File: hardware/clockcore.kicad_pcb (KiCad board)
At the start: 2 copper layers, 75 x 40 mm, 38 parts, among them J1 Header, J2 USB_C_Receptacle_USB2.0, J3 JTAG Debug Header, Q1 MBT3904DW1T1G, SW1 Reset, SW2 Boot, U1 ESP32-WROOM-32, U2 DS1338Z-33+, U3 FT231XS, U4 USBLC6-4SC6, U5 ‎SN74HCT245PWR‎, Y1 32.768Hz, 12.5pF, 45kΩ

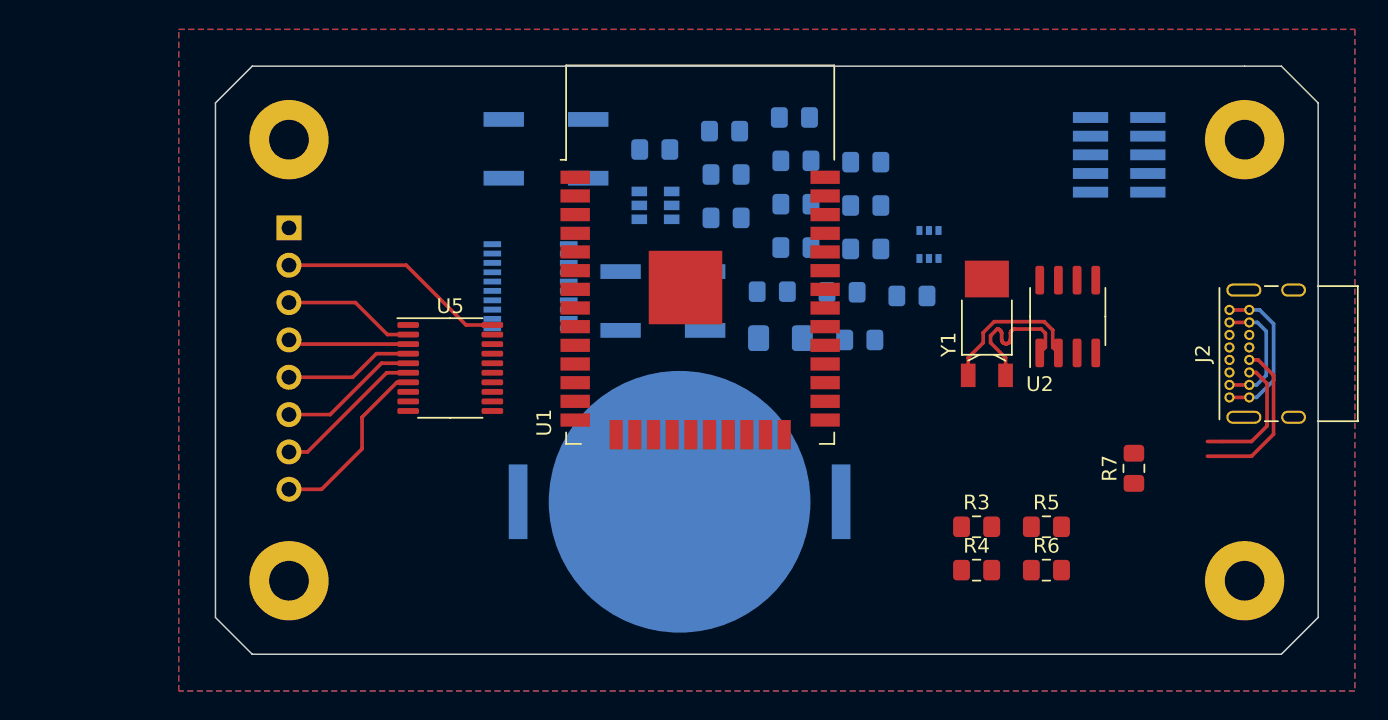
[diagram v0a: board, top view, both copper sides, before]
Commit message: finished schematic for clockcore, pcb layout todo
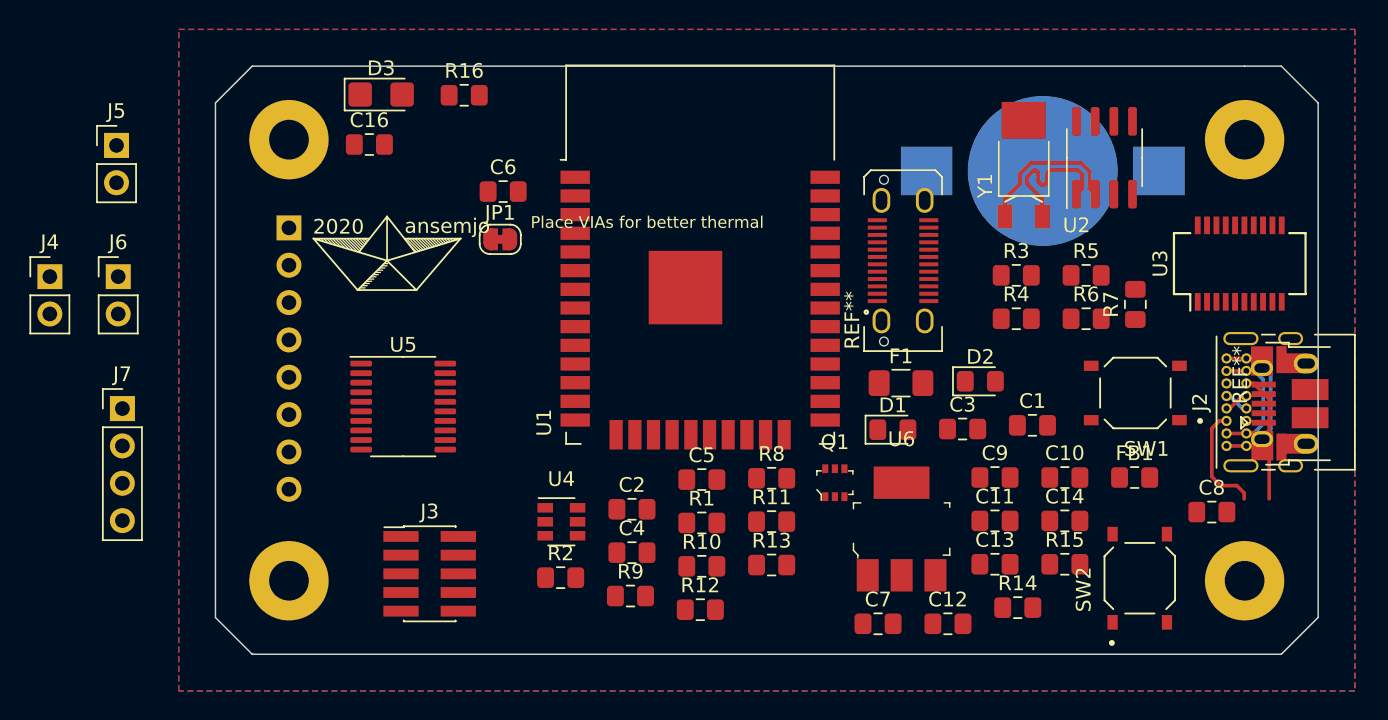
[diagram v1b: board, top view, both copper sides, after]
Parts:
- added A1: 2020, extra_libraries:AHOI, F.Cu at (96.7, 60.7)
- added C10: 4.7µF, Capacitor_SMD:C_0805_2012Metric_Pad1.15x1.40mm_HandSolder, F.Cu at (142.8, 75.5)
- added C11: 100nF, Capacitor_SMD:C_0805_2012Metric_Pad1.15x1.40mm_HandSolder, F.Cu at (138.0, 78.4)
- added C12: 10µF, Capacitor_SMD:C_0805_2012Metric_Pad1.15x1.40mm_HandSolder, F.Cu at (134.8, 85.4)
- added C13: 100nF, Capacitor_SMD:C_0805_2012Metric_Pad1.15x1.40mm_HandSolder, F.Cu at (138.0, 81.4)
- added C14: DNP/100nF, Capacitor_SMD:C_0805_2012Metric_Pad1.15x1.40mm_HandSolder, F.Cu at (142.8, 78.4)
- added C16: 1nF, Capacitor_SMD:C_0805_2012Metric_Pad1.15x1.40mm_HandSolder, F.Cu at (95.5, 52.8)
- added C6: 10nF, Capacitor_SMD:C_0805_2012Metric_Pad1.15x1.40mm_HandSolder, F.Cu at (104.6, 56.0)
- added C7: 4.7µF, Capacitor_SMD:C_0805_2012Metric_Pad1.15x1.40mm_HandSolder, F.Cu at (130.1, 85.4)
- added C8: 100nF, Capacitor_SMD:C_0805_2012Metric_Pad1.15x1.40mm_HandSolder, F.Cu at (152.8, 77.8)
- added C9: 4.7µF, Capacitor_SMD:C_0805_2012Metric_Pad1.15x1.40mm_HandSolder, F.Cu at (138.0, 75.5)
- added D3: Ambient Light Sensor, Diode_SMD:D_1206_3216Metric_Castellated, F.Cu at (96.3, 49.4)
- added FB1: BLM21PG221SZ1D, Inductor_SMD:L_0805_2012Metric_Pad1.15x1.40mm_HandSolder, F.Cu at (147.5, 75.5)
- added J4: 3.3V, Connector_PinHeader_2.54mm:PinHeader_1x02_P2.54mm_Vertical, F.Cu at (73.7, 61.8)
- added J5: 5V, Connector_PinHeader_2.54mm:PinHeader_1x02_P2.54mm_Vertical, F.Cu at (78.3, 52.9)
- added J6: I2C, Connector_PinHeader_2.54mm:PinHeader_1x02_P2.54mm_Vertical, F.Cu at (78.4, 61.8)
- added J7: Serial Prog, Connector_PinHeader_2.54mm:PinHeader_1x04_P2.54mm_Vertical, F.Cu at (78.7, 70.8)
- added JP1: Bridge, Jumper:SolderJumper-2_P1.3mm_Bridged_RoundedPad1.0x1.5mm, F.Cu at (104.4, 59.3)
- added R14: 10kΩ, Resistor_SMD:R_0805_2012Metric_Pad1.15x1.40mm_HandSolder, F.Cu at (139.6, 84.3)
- added R15: 10kΩ, Resistor_SMD:R_0805_2012Metric_Pad1.15x1.40mm_HandSolder, F.Cu at (142.8, 81.4)
- added R16: 4.7kΩ, Resistor_SMD:R_0805_2012Metric_Pad1.15x1.40mm_HandSolder, F.Cu at (101.9, 49.5)
- added REF**: USB_Micro-B_Amphenol_10103594-0001LF_Horizontal, Connector_USB:USB_Micro-B_Amphenol_10103594-0001LF_Horizontal, F.Cu at (158.1, 70.4)
- added REF**: USB_C_Receptacle_JAE_DX07S024WJ3R400, Connector_USB:USB_C_Receptacle_JAE_DX07S024WJ3R400, F.Cu at (131.8, 60.7)
- added U6: AP2114H-3_3TRG1, digikey-footprints:SOT-223, F.Cu at (131.7, 79.0)
- BT1: value 20mm Coin Cell -> 12mm Coin Cell; footprint Battery:BatteryHolder_Keystone_3034_1x20mm -> Battery:BatteryHolder_Keystone_3000_1x12mm
- C1, C2, C3, C4, C5, D1, D2, F1, Q1, R1, R10, R11, R12, R13, R2, R8, R9, U3, U4: moved to F.Cu
- J3: value JTAG Debug Header -> JTAG; moved to F.Cu
- SW1, SW2: footprint Button_Switch_SMD:SW_SPST_B3SL-1002P -> extra_libraries:SW_PTS526_SM08_SMTR2_LFS; moved to F.Cu
- moved J3 54.9 mm to (99.6, 82.0)
- moved SW2 49.8 mm to (147.9, 82.3), turned to 90 degrees
- moved U3 48.3 mm to (154.7, 60.9), turned to 90 degrees
- moved R12 34.1 mm to (118.0, 84.5)
- moved BT1 33.4 mm to (141.3, 54.6), turned to 0 degrees
- moved SW1 32.7 mm to (147.6, 69.7), turned to 180 degrees
- moved R9 32.3 mm to (113.2, 83.5)
- moved R2 29.8 mm to (108.5, 82.3)
- moved R10 28.3 mm to (118.1, 81.5)
- moved R13 28.1 mm to (122.8, 81.4)
- moved C4 26.5 mm to (113.3, 80.6)
- moved R1 22.6 mm to (118.1, 78.6)
- moved U4 22.5 mm to (108.5, 78.5)
- moved R11 22.4 mm to (122.8, 78.5)
- moved C2 20.8 mm to (113.3, 77.6)
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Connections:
- net FIL_SHDN renamed /FIL_SHDN
- net HV_BLANK renamed /HV_BLANK
- net HV_CLOCK renamed /HV_CLOCK
- net HV_DATA renamed /HV_DATA
- net HV_STROBE renamed /HV_STROBE
- net ~HV_SHDN~ renamed /~HV_SHDN~
- D1 pad 2: +3V3 -> Net-(D1-Pad2)
- J2 pad A4: Net-(F1-Pad2) -> VBUS
- J2 pad A9: Net-(F1-Pad2) -> VBUS
- J2 pad B4: Net-(F1-Pad2) -> VBUS
- J2 pad B9: Net-(F1-Pad2) -> VBUS
- J2 pad S1: GND -> Net-(C14-Pad1)
- J3 pad 1: (no net) -> +3V3
- J3 pad 10: (no net) -> CHIP_EN
- J3 pad 2: (no net) -> JTAG_TMS
- J3 pad 3: Net-(J3-Pad3) -> GND
- J3 pad 4: (no net) -> JTAG_TCK
- J3 pad 5: Net-(J3-Pad3) -> GND
- J3 pad 6: (no net) -> JTAG_TDO
- J3 pad 8: (no net) -> JTAG_TDI
- J3 pad 9: (no net) -> GND
- U1 pad 10: (no net) -> IO_CLOCK
- U1 pad 11: (no net) -> IO_DATA
- U1 pad 12: (no net) -> IO_STROBE
- U1 pad 13: (no net) -> JTAG_TMS
- U1 pad 14: (no net) -> JTAG_TDI
- U1 pad 16: (no net) -> JTAG_TCK
- U1 pad 23: (no net) -> JTAG_TDO
- U1 pad 25: (no net) -> GPIO0
- U1 pad 27: (no net) -> ~IO_HV_SHDN~
- U1 pad 28: (no net) -> IO_FIL_SHDN
- U1 pad 30: (no net) -> IO_BLANK
- U1 pad 31: (no net) -> ~OUTPUT_EN~
- U1 pad 4: (no net) -> LIGHT
- U1 pad 8: (no net) -> Net-(C16-Pad1)
- U1 pad 9: (no net) -> RTC_SQW
- U5 pad 13: (no net) -> ~IO_HV_SHDN~
- U5 pad 14: (no net) -> IO_FIL_SHDN
- U5 pad 15: (no net) -> IO_BLANK
- U5 pad 16: (no net) -> IO_STROBE
- U5 pad 17: (no net) -> IO_DATA
- U5 pad 18: (no net) -> IO_CLOCK
- U5 pad 19: (no net) -> ~OUTPUT_EN~
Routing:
- net +5V: track 15.5 -> 0.00 mm
- net /~HV_SHDN~: track 12.4 -> 0.00 mm
- net /FIL_SHDN: track 10.3 -> 0.00 mm
- net /HV_BLANK: track 9.56 -> 0.00 mm
- net /D-: track 11.2 -> 1.70 mm
- net /HV_CLOCK: track 9.01 -> 0.00 mm
- net Net-(J2-PadB8): track 8.90 -> 0.00 mm
- net /CC2: track 0.00 -> 8.78 mm
- net /HV_STROBE: track 8.77 -> 0.00 mm
- net Net-(F1-Pad2): track 8.51 -> 0.00 mm
- net VBUS: track 0.00 -> 8.51 mm
- net /HV_DATA: track 8.23 -> 0.00 mm
- net /CC1: track 0.00 -> 7.56 mm
- net /D+: track 0.00 -> 1.70 mm
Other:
- board text added: "Place VIAs for better thermal"

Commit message: finished pcb routing for clockcore, forgot to add zener
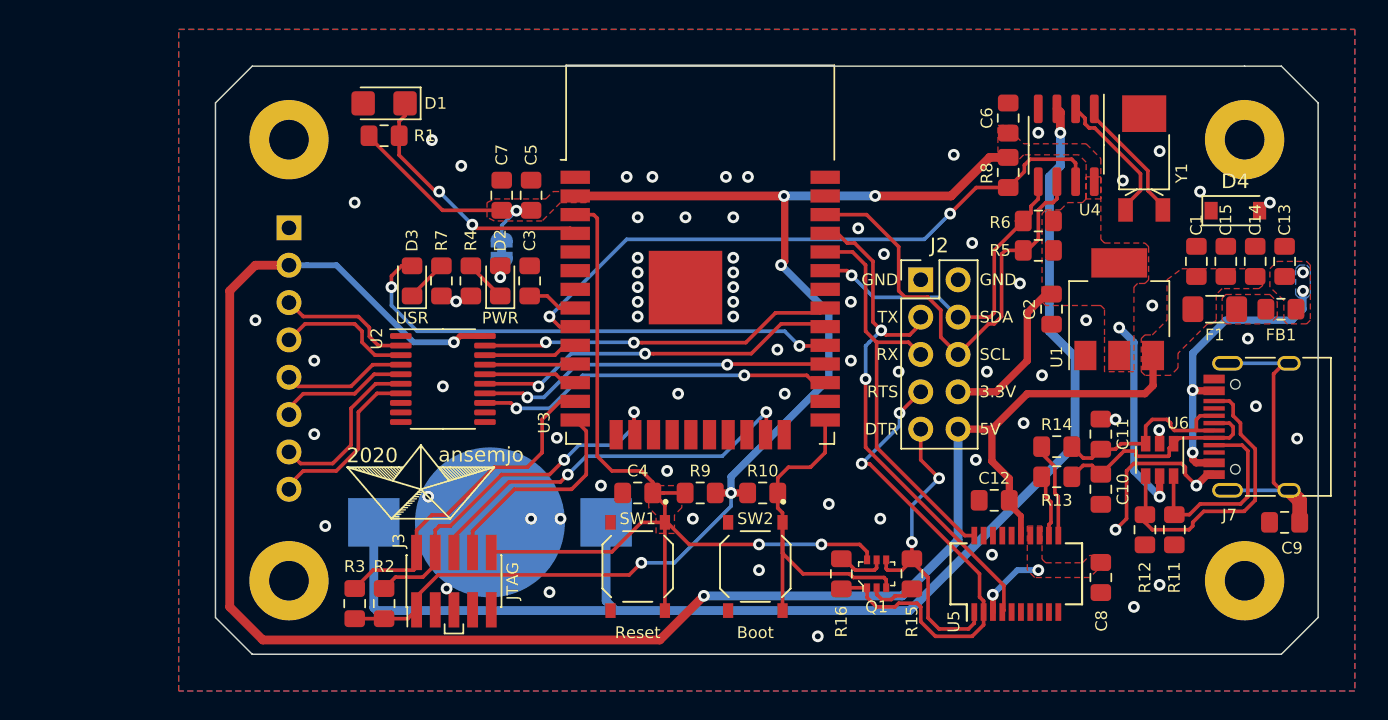
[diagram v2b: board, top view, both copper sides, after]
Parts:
- removed the C10 at (142.8, 75.5)
- removed the C11 at (138.0, 78.4)
- removed C16: 1nF, Capacitor_SMD:C_0805_2012Metric_Pad1.15x1.40mm_HandSolder
- removed the C6 at (104.6, 56.0)
- removed the C7 at (130.1, 85.4)
- removed the C8 at (152.8, 77.8)
- removed the C9 at (138.0, 75.5)
- removed J4: 3.3V, Connector_PinHeader_2.54mm:PinHeader_1x02_P2.54mm_Vertical
- removed J5: 5V, Connector_PinHeader_2.54mm:PinHeader_1x02_P2.54mm_Vertical
- removed J6: I2C, Connector_PinHeader_2.54mm:PinHeader_1x02_P2.54mm_Vertical
- removed the J7 at (78.7, 70.8)
- removed the R1 at (118.1, 78.6)
- removed the R10 at (118.1, 81.5)
- removed the R12 at (118.0, 84.5)
- removed the R2 at (108.5, 82.3)
- removed the R8 at (122.8, 75.5)
- removed REF**: USB_Micro-B_Amphenol_10103594-0001LF_Horizontal, Connector_USB:USB_Micro-B_Amphenol_10103594-0001LF_Horizontal
- removed REF**: USB_C_Receptacle_JAE_DX07S024WJ3R400, Connector_USB:USB_C_Receptacle_JAE_DX07S024WJ3R400
- removed the U4 at (108.5, 78.5)
- added A2: Logo_Open_Hardware_Small, Symbol:OSHW-Logo2_7.3x6mm_SilkScreen, B.Cu at (148.0, 82.5)
- added C1: 4.7µF, Capacitor_SMD:C_0805_2012Metric_Pad1.15x1.40mm_HandSolder, F.Cu at (151.7, 60.8)
- added C13: 10nF, Capacitor_SMD:C_0805_2012Metric_Pad1.15x1.40mm_HandSolder, F.Cu at (157.7, 60.8)
- added C14: 100nF, Capacitor_SMD:C_0805_2012Metric_Pad1.15x1.40mm_HandSolder, F.Cu at (155.7, 60.8)
- added C15: 4.7µF, Capacitor_SMD:C_0805_2012Metric_Pad1.15x1.40mm_HandSolder, F.Cu at (153.7, 60.8)
- added C2: 4.7µF, Capacitor_SMD:C_0805_2012Metric_Pad1.15x1.40mm_HandSolder, F.Cu at (141.9, 64.0)
- added C3: 1nF, Capacitor_SMD:C_0805_2012Metric_Pad1.15x1.40mm_HandSolder, F.Cu at (106.4, 62.1)
- added C4: 100nF, Capacitor_SMD:C_0805_2012Metric_Pad1.15x1.40mm_HandSolder, F.Cu at (113.7, 76.5)
- added D4: 1N5819HW, Diode_SMD:D_SOD-123, F.Cu at (154.4, 57.3)
- added J2: Ext, Connector_PinHeader_2.54mm:PinHeader_2x05_P2.54mm_Vertical, F.Cu at (133.0, 62.0)
- added R14: 27Ω, Resistor_SMD:R_0805_2012Metric_Pad1.15x1.40mm_HandSolder, F.Cu at (142.2, 73.4)
- added R16: 10kΩ, Resistor_SMD:R_0805_2012Metric_Pad1.15x1.40mm_HandSolder, F.Cu at (127.6, 82.0)
- added R3: 10kΩ, Resistor_SMD:R_0805_2012Metric_Pad1.15x1.40mm_HandSolder, F.Cu at (94.5, 84.1)
- added R4: 1kΩ, Resistor_SMD:R_0805_2012Metric_Pad1.15x1.40mm_HandSolder, F.Cu at (102.4, 62.1)
- added R7: 1kΩ, Resistor_SMD:R_0805_2012Metric_Pad1.15x1.40mm_HandSolder, F.Cu at (100.4, 62.1)
- added U6: USBLC6-4SC6, Package_TO_SOT_SMD:SOT-23-6, F.Cu at (149.2, 74.3)
- D1: value PWR LED -> Ambient Light Sensor; footprint LED_SMD:LED_0805_2012Metric_Pad1.15x1.40mm_HandSolder -> Diode_SMD:D_1206_3216Metric_Castellated
- D2: value GPIO LED -> PWR LED
- D3: value Ambient Light Sensor -> GPIO LED; footprint Diode_SMD:D_1206_3216Metric_Castellated -> LED_SMD:LED_0805_2012Metric_Pad1.15x1.40mm_HandSolder
- FB1: value BLM21PG221SZ1D -> 220ΩZ
- J3: footprint Connector_PinHeader_1.27mm:PinHeader_2x05_P1.27mm_Vertical_SMD -> extra_libraries:JTAG_2x05_P1.27mm_Vertical_SMD
- J7: renamed from J2; value USB_C_Receptacle_USB2.0 -> GCT_USB4108-GF-A; footprint Connector_USB:USB_C_Receptacle_GCT_USB4085 -> Connector_USB:USB_C_Receptacle_HRO_TYPE-C-31-M-12
- JP1: moved to B.Cu
- U1: renamed from U6; footprint digikey-footprints:SOT-223 -> Package_TO_SOT_SMD:SOT-223
- moved BT1 44.6 mm to (103.7, 78.5)
- moved R2 43.1 mm to (96.5, 84.1), turned to 90 degrees
- moved C7 41.9 mm to (104.5, 56.3), turned to 90 degrees
- moved D1 41.1 mm to (96.5, 50.0), turned to 180 degrees
- moved C5 40.7 mm to (106.5, 56.3), turned to 90 degrees
- moved SW1 35.8 mm to (113.7, 81.5), turned to 270 degrees
- moved D2 33.4 mm to (104.4, 62.1), turned to 90 degrees
- moved C8 32.2 mm to (145.2, 82.3), turned to 270 degrees
- moved C10 32.2 mm to (145.2, 76.3), turned to 270 degrees
- moved C11 27.3 mm to (145.2, 72.5), turned to 90 degrees
- moved SW2 26.2 mm to (121.7, 81.5), turned to 270 degrees
- moved U5 26.0 mm to (139.5, 82.0)
- moved F1 21.9 mm to (153.0, 64.0)
- moved U1 21.0 mm to (146.5, 64.0), turned to 90 degrees
- moved C6 21.0 mm to (138.9, 51.0), turned to 90 degrees
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- renumbered C4 to C10, C5 to C11, C3 to C12, C12 to C5, C1 to C6, C13 to C7, C2 to C8, C14 to C9, R16 to R1, R11 to R10, R3 to R11, R4 to R12, R14 to R2, R7 to R8, U5 to U2, U1 to U3, U2 to U4, U3 to U5
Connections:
- D1 pad 1: Net-(D1-Pad1) -> LIGHT
- D1 pad 2: Net-(D1-Pad2) -> GND
- D2 pad 2: IO_LED -> Net-(D2-Pad2)
- D3 pad 1: LIGHT -> Net-(D3-Pad1)
- D3 pad 2: GND -> IO_LED
- F1 pad 1: +5V -> Net-(D4-Pad2)
- J3 pad 9: GND -> (no net)
- JP1 pad 2: Net-(D1-Pad2) -> Net-(D2-Pad2)
- R13 pad 1: USB+ -> USB-
- R13 pad 2: /D+ -> /D-
- R15 pad 1: +3V3 -> DTR
- R15 pad 2: JTAG_TMS -> Net-(Q1-Pad2)
- R9 pad 1: DTR -> +3V3
- R9 pad 2: Net-(Q1-Pad2) -> CHIP_EN
- U5 pad 20: TXD0 -> RXD0
- U5 pad 4: RXD0 -> TXD0
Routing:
- net +5V: track 0.00 -> 127.4 mm, vias 0 -> 2
- net +3V3: track 0.00 -> 127.0 mm, vias 0 -> 8
- net Net-(BT1-Pad1): track 0.00 -> 88.5 mm, vias 0 -> 1
- net CHIP_EN: track 0.00 -> 61.3 mm, vias 0 -> 2
- net RTC_SQW: track 0.00 -> 43.9 mm, vias 0 -> 2
- net TXD0: track 0.00 -> 36.1 mm, vias 0 -> 2
- net IO_LED: track 0.00 -> 34.9 mm, vias 0 -> 2
- net RTS: track 0.00 -> 33.9 mm, vias 0 -> 2
- net SCL: track 0.00 -> 31.7 mm
- net RXD0: track 0.00 -> 28.3 mm
- net JTAG_TDO: track 0.00 -> 27.4 mm, vias 0 -> 2
- net GPIO0: track 0.00 -> 25.8 mm
- net JTAG_TCK: track 0.00 -> 25.5 mm, vias 0 -> 2
- net IO_BLANK: track 0.00 -> 25.0 mm, vias 0 -> 2
- net ~IO_HV_SHDN~: track 0.00 -> 24.4 mm, vias 0 -> 2
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- added copper zone on F.Cu, net +3V3
- added copper zone on F.Cu, net +5V
- added copper zone on F.Cu, net /FT231_LDO
- added copper zone on F.Cu, net CHIP_EN
- added copper zone on F.Cu, net Net-(F1-Pad2)
- added copper zone on B.Cu, net VBUS
- added copper zone on F.Cu, net VBUS
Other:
- net class Default: clearance 0.25 -> 0.2
- rule trace_clearance: 0.25 -> 0.2
- board text added: "3.3V"
- board text added: "Boot"
- board text added: "CR1225"
- board text added: "Clock Core v1.0 github.com/ansemjo/chronovfd"
- board text added: "DTR"
- board text added: "JTAG"
- board text added: "PWR"
- board text added: "RTS"
- board text added: "RX"
- board text added: "Reset"
- board text added: "SCL"
- board text added: "SDA"
- board text added: "TODO --------------- - teardrops"
- board text added: "TX"
- board text added: "USR"
- board text added: "cut jumper to disable PWR LED"
- board text added: "to ИВЛ2-7/5 driver"
- board text removed: "Place VIAs for better thermal"
- board text removed: "blank"
- board text removed: "clock"
- board text removed: "data"
- board text removed: "filShdn"
- board text removed: "strobe"
- board text removed: "~hvShdn~"

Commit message: final clockcore design v2_copy ... i think
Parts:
- added REF**: RF_Hazard, extra_libraries:RF_Hazard, F.Cu at (130.4, 51.1)
- A2: footprint Symbol:OSHW-Logo2_7.3x6mm_SilkScreen -> Symbol:OSHW-Symbol_6.7x6mm_SilkScreen
- BT1: footprint Battery:BatteryHolder_Keystone_3000_1x12mm -> Battery:BatteryHolder_Keystone_1058_1x2032
- moved BT1 6.71 mm to (109.6, 75.3)
- moved C14 5.67 mm to (152.0, 65.0), turned to 0 degrees
- moved F1 4.78 mm to (156.5, 60.8), turned to 180 degrees
- moved C13 4.60 mm to (156.0, 65.0), turned to 180 degrees
- moved C15 2.85 mm to (152.0, 63.0), turned to 0 degrees
- moved FB1 1.80 mm to (156.0, 63.0)
- moved U1 1.41 mm to (145.5, 65.0)
- moved C2 1.15 mm to (140.7, 64.0)
- moved D4 1.12 mm to (155.0, 58.3)
- moved A1 1.05 mm to (97.9, 76.3)
- moved R5 1.00 mm to (140.0, 60.0)
- moved R6 1.00 mm to (140.0, 58.0)
- moved A2 0.92 mm to (148.2, 81.6)
- moved C1 0.35 mm to (152.0, 61.0), turned to 0 degrees
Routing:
- net Net-(BT1-Pad1): track 88.5 -> 83.9 mm
- net Net-(D4-Pad2): track 0.00 -> 3.55 mm
- net Net-(F1-Pad2): track 0.00 -> 2.27 mm
- net +5V: track 127.4 -> 125.4 mm
- net SDA: track 23.6 -> 22.0 mm
- net GND: vias 71 -> 72
- removed copper zone on F.Cu, net Net-(F1-Pad2)
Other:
- board text added: ""screw it, put a chip in it.""
- board text added: "- @internetofshit"
- board text added: "CR2032"
- board text added: "WARRANTY VOID"
- board text removed: "CR1225"
- board text removed: "TODO --------------- - teardrops"
